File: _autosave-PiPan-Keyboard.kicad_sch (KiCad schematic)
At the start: 89 parts

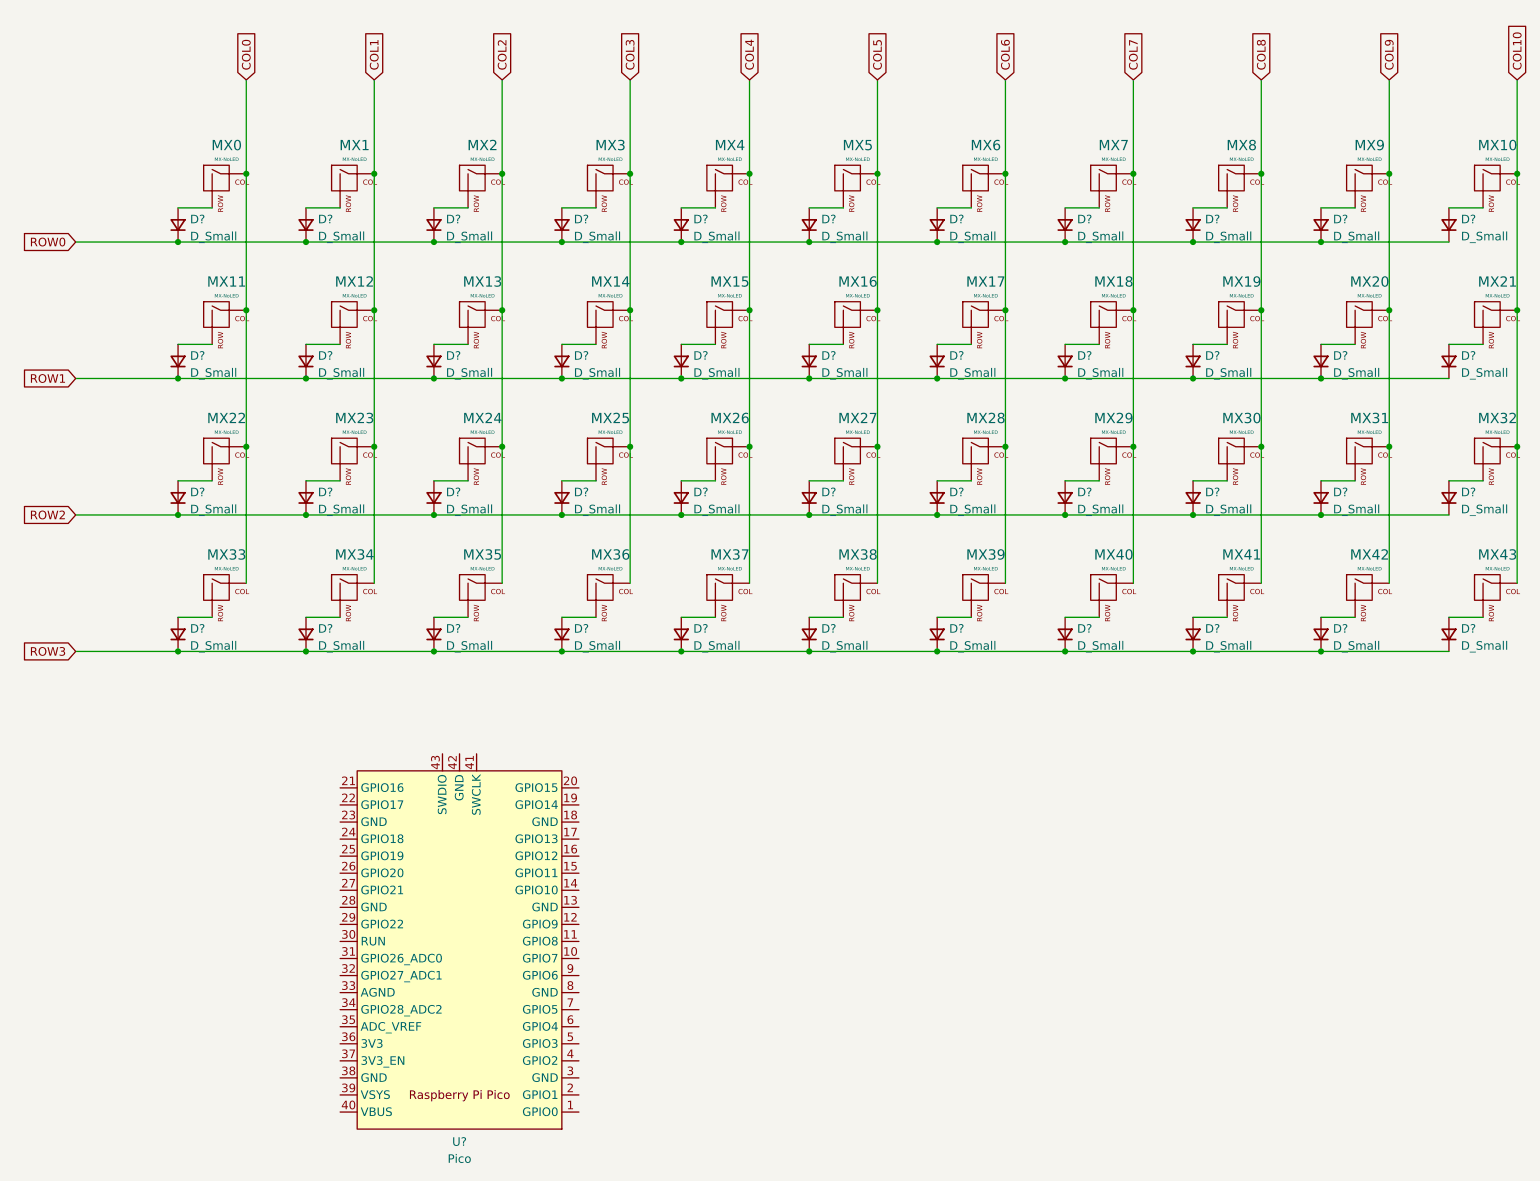
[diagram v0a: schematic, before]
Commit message: added digikey lib
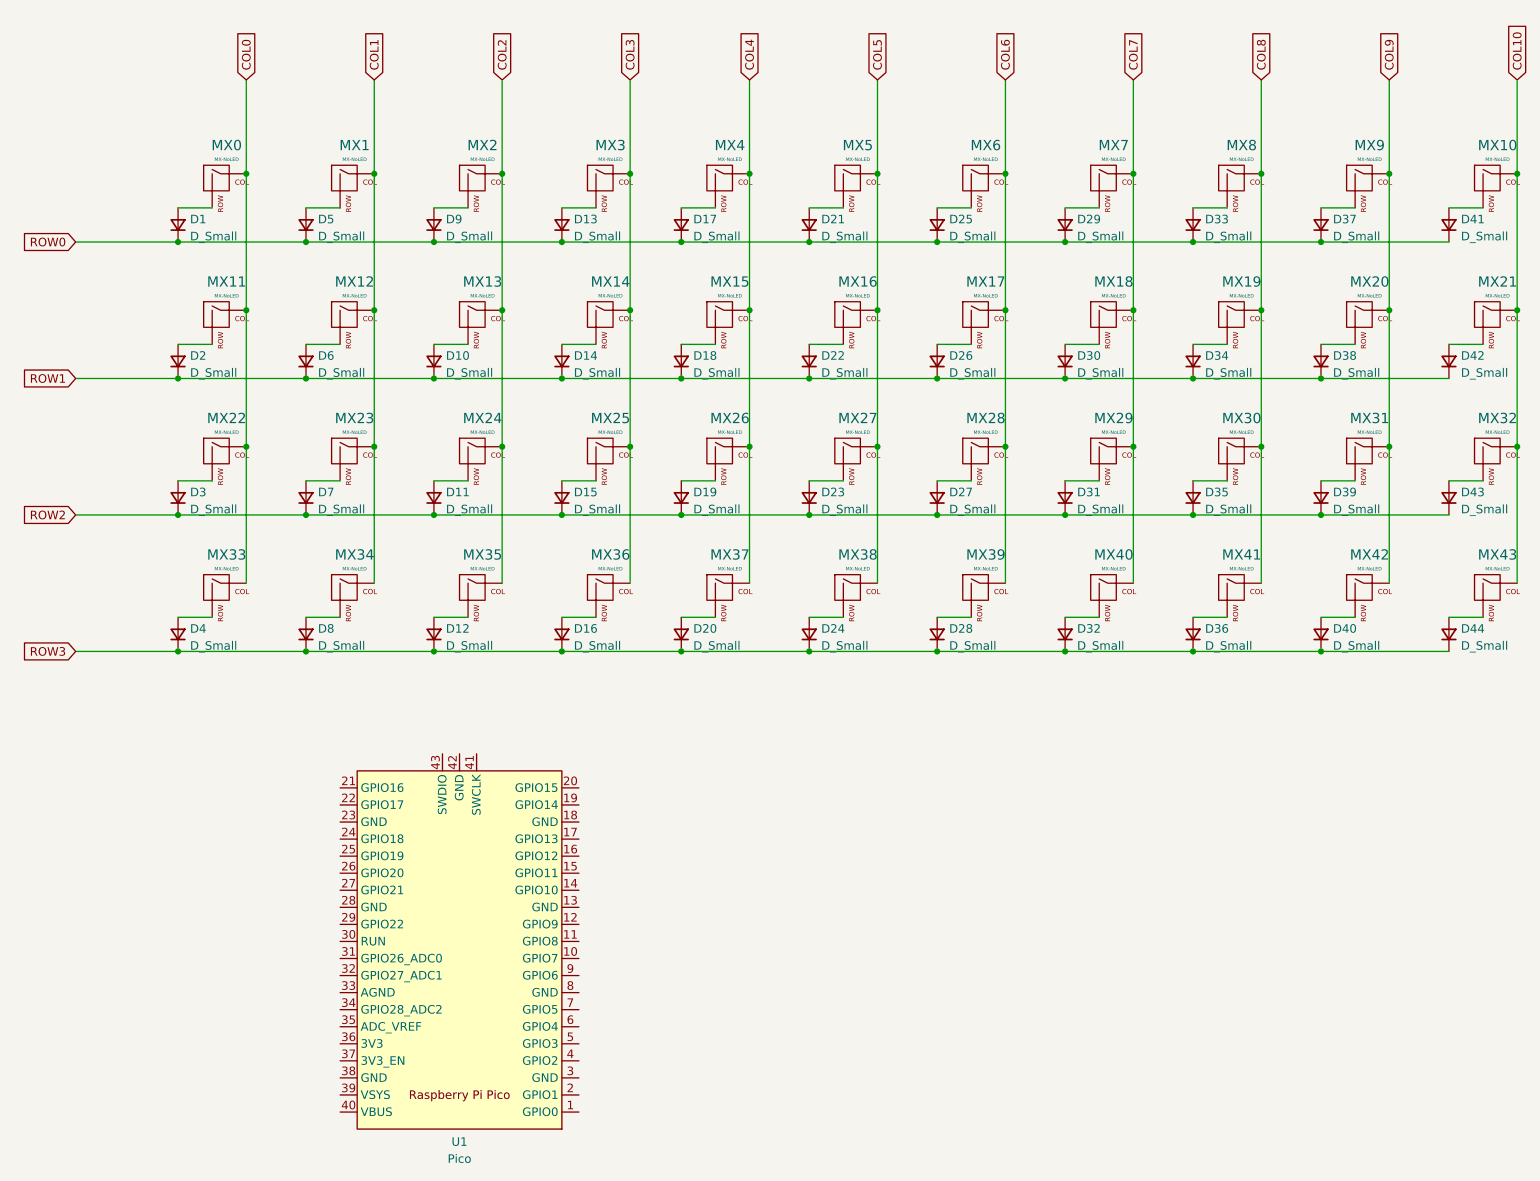
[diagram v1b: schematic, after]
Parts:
- gave numbers to parts that had none: 45
